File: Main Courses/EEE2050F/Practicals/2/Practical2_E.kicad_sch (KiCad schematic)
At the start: 3 parts, among them IC1 4049, IC2 4081, IC3 4071

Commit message: Complete schematic 2
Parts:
- added C1: 10µF, symbol Device:C_Polarized
- added C2, C3, C4: 10nF, symbol Device:C
- added D1: LED, symbol Device:LED
- added unit 3 of IC1
- added unit 2 of IC1
- added unit 7 of IC1
- added unit 4 of IC1
- added unit 4 of IC2
- added unit 5 of IC2
- added unit 2 of IC2
- added unit 3 of IC2
- added unit 4 of IC3
- added unit 2 of IC3
- added unit 5 of IC3
- added unit 3 of IC3
- added R1: 150, symbol Device:R
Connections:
- new net: D1.2 (A), R1.2
- new net +5V: C1.1, C2.1, C3.1, C4.1, IC1.1 (VCC), IC2.14 (VDD), IC3.14 (VDD), R1.1
- new net GND: C1.2, C2.2, C3.2, C4.2, D1.1 (K), IC1.5, IC1.7, IC1.8 (VSS), IC1.9, IC2.12, IC2.13, IC2.5, IC2.6, IC2.7 (VSS), IC2.8, IC2.9, IC3.12, IC3.13, IC3.5, IC3.6, IC3.7 (VSS), IC3.8, IC3.9
- no-connect marks 0 -> 9
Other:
- moved on the sheet: IC1A, IC2A, IC3A

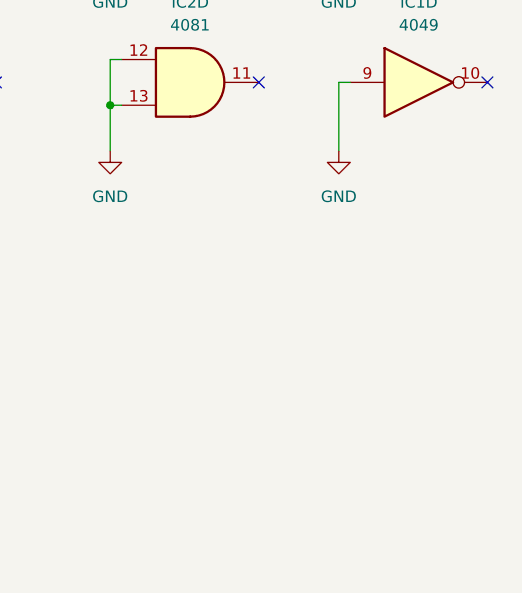
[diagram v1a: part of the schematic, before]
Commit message: Add missing CD4049 gates
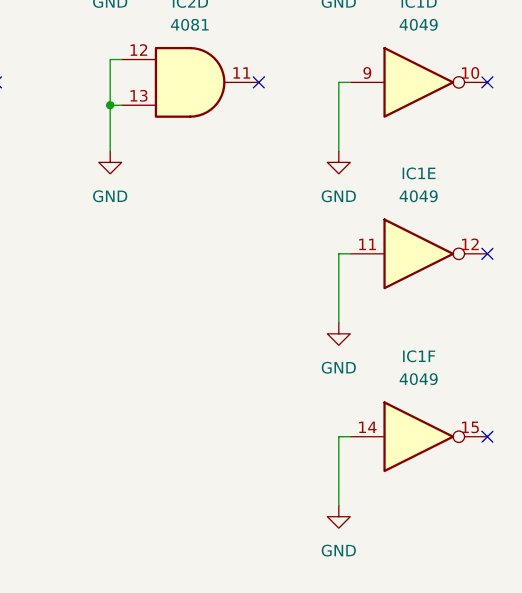
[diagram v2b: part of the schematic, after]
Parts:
- added unit 6 of IC1
- added unit 5 of IC1
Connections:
- net GND: now also IC1.11, IC1.14
- no-connect marks 9 -> 11
